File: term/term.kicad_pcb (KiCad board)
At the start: 2 copper layers, 35.6 x 30.5 mm, 39 parts, among them P101 CONN_01X08, P102 XG4C-1631, P103 CONN_01X08, SW101 SW_PUSH

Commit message: Fix terminator board to point to 5.1 symbol libraries.
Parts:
- W101, W102: value TEST_1P -> TestPoint
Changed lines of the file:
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@@
       (effects (font (size 1 1) (thickness 0.15)))
     )
-    (fp_text value TEST_1P (at -1.905 3.175) (layer F.Fab)
+    (fp_text value TestPoint (at -1.905 3.175) (layer F.Fab)
       (effects (font (size 1 1) (thickness 0.15)))
     )
@@
       (effects (font (size 1 1) (thickness 0.15)))
     )
-    (fp_text value TEST_1P (at -1.905 3.175) (layer F.Fab)
+    (fp_text value TestPoint (at -1.905 3.175) (layer F.Fab)
       (effects (font (size 1 1) (thickness 0.15)))
     )

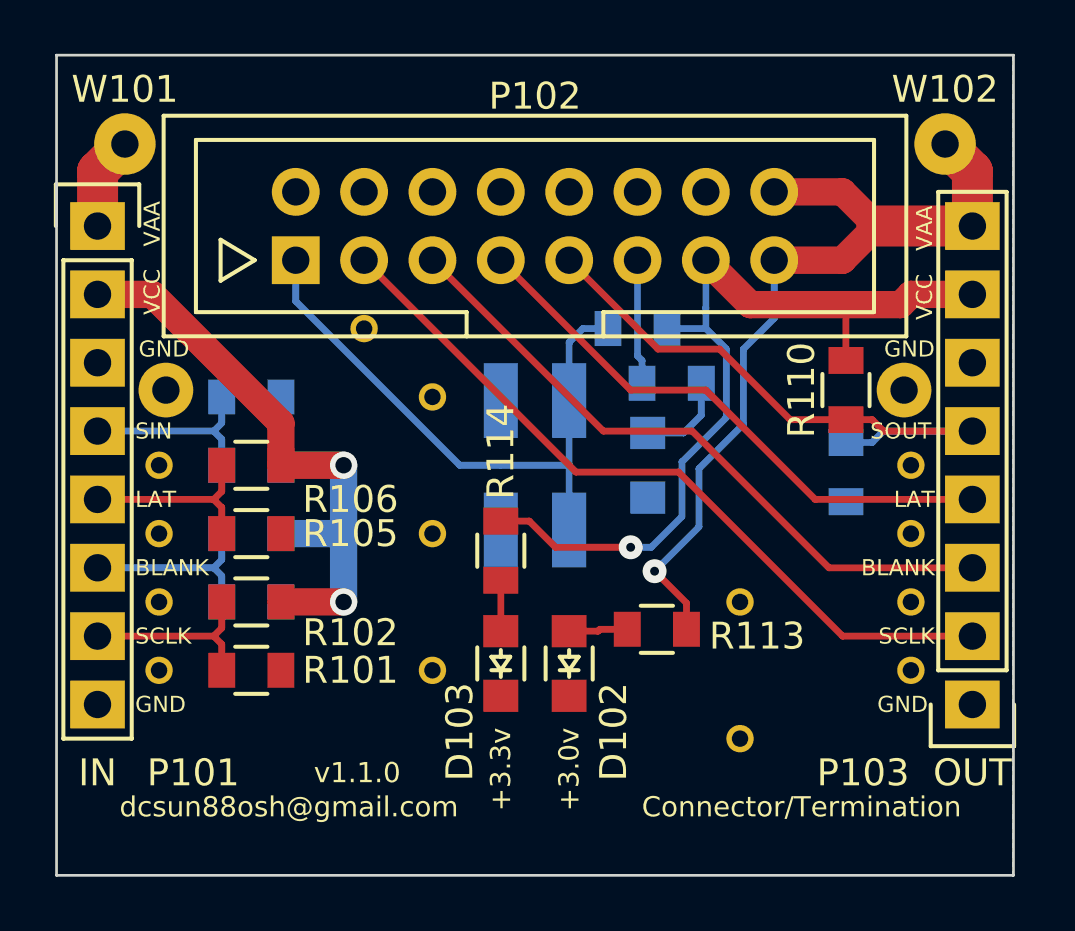
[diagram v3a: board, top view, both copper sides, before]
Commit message: Update term design to KiCad 8.
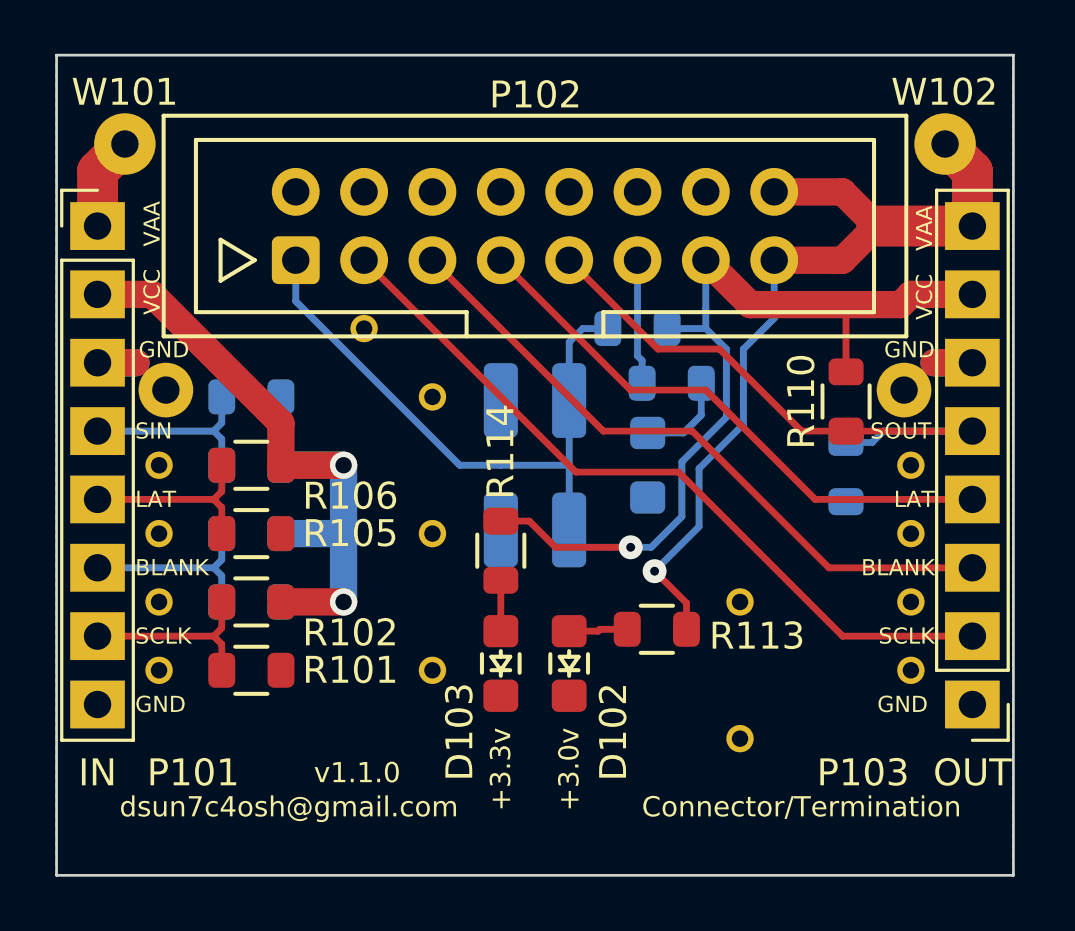
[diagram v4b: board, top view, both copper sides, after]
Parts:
- D101, D102, D103: footprint local:LED_0805_HandSoldering -> Local:LED_0805_HandSoldering
- P101, P103: footprint local:Pin_Header_1x08_square -> Local:Pin_Header_1x08_square
- P102: footprint local:XG4C-1631 -> Local:XG4C-1631
- R101, R102, R103, R104, R105, R106, R107, R108, R109, R110, R111, R112, R113, R114: footprint local:R_0805_HandSoldering -> Local:R_0805_HandSoldering
- REF** (x14): footprint local:Stitching_Via_40x24mil -> Local:Stitching_Via_40x24mil
- REF** (x2): value Stitching_Via_40x24mil -> Stitching_Via_80x40mil; footprint local:Stitching_Via_40x24mil -> Local:Stitching_Via_80x40mil
- SW101: footprint local:7914J_HandSoldering -> Local:7914J_HandSoldering
- W101, W102: footprint Wire_Pads:SolderWirePad_single_1mmDrill -> Local:wire_90x40mil
- moved P102 8.98 mm to (135.9, 91.4), turned to 90 degrees
- moved R110 0.42 mm to (156.3, 96.7)
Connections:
- net /~RESET~ renamed /~{RESET}
- P102 pad 2: Net-(P102-Pad2) -> unconnected-(P102-Pin_2-Pad2)
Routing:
- net GND: track 0.00 -> 5.70 mm
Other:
- net class Default removed
- net class minimum removed
- rule pad_to_mask_clearance: 0 -> 0.0508
- board text added: "dsun7c4osh@gmail.com"
- board text removed: "dcsun88osh@gmail.com"

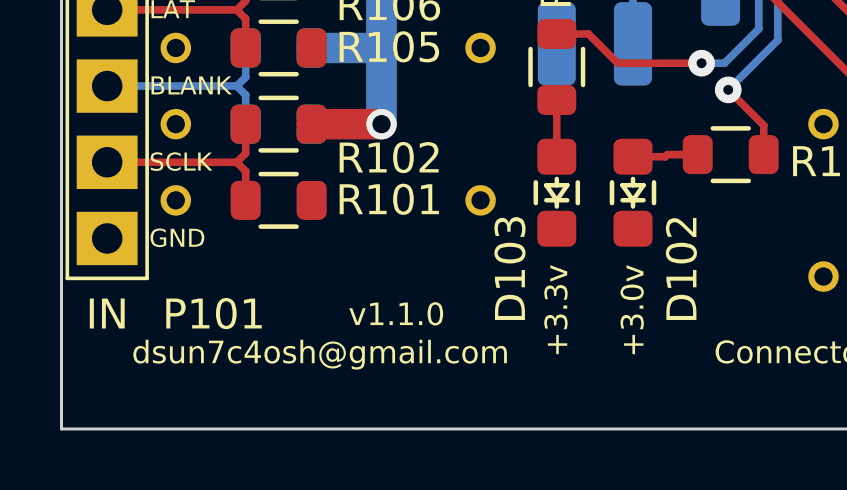
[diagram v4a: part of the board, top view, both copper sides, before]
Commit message: Bump version string of term to v1.2.0.
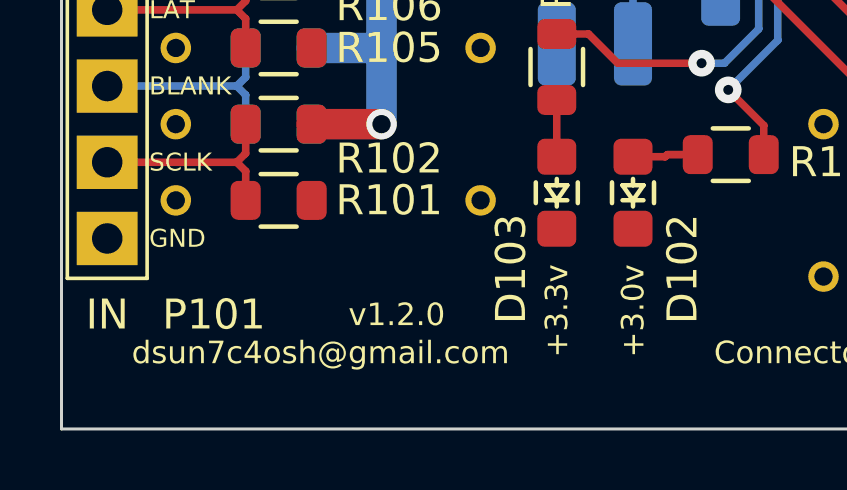
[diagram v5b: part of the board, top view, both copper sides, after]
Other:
- board text added: "v1.2.0"
- board text removed: "v1.1.0"
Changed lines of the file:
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@@
 	)
 	(paper "A4")
+	(title_block
+		(title "Connector/Terminator")
+		(date "2025-01-27")
+		(rev "v1.2.0")
+	)
 	(layers
 		(0 "F.Cu" signal)
@@
 		)
 	)
-	(gr_text "v1.1.0"
+	(gr_text "v1.2.0"
 		(at 138.176 110.49 0)
 		(layer "F.SilkS")
